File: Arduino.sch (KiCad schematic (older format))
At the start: 0 parts

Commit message: Hooked up top level schematic
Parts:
- added ARD?: ARDUINO_PINS, symbol ARDUINO_PINS
- added R? (x13): R, ~, symbol R
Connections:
- net MISO: now also R?.2
- net MOSI: now also R?.2
- net SCLK: now also R?.2
- net Tach_Meas: now also R?.1
- new net: ARD?.11 (DIGITAL_0_RX), R?.1
- new net: ARD?.12 (DIGITAL_1_TX), R?.1
- new net: ARD?.18 (DIGITAL_7), R?.1
- new net: ARD?.19 (DIGITAL_8), R?.1
- new net: ARD?.20 (DIGITAL_9_CS), R?.1
- new net: ARD?.21 (DIGITAL_10_MOSI), R?.1
- new net: ARD?.22 (DIGITAL_11_MISO), R?.1
- new net: ARD?.23 (DIGITAL_12_SCK), R?.1
- new net: ARD?.5 (ANALOG_0), R?.2
- new net: ARD?.6 (ANALOG_1), R?.2
- new net: ARD?.7 (ANALOG_2), R?.2
- new net: ARD?.8 (ANALOG_3), R?.2
- new net ADC_CS_N: R?.2
- new net CURR_MEAS: R?.1
- new net DAC_CS_N: R?.2
- new net Fan_En_N: R?.2
- new net GND: R?.1
- new net LED_EN_PWM: R?.2
- new net RELAY+: R?.2
- new net RELAY-: R?.2
- new net V+_ADJ_MON: R?.1
- new net V-_ADJ_MON: R?.1

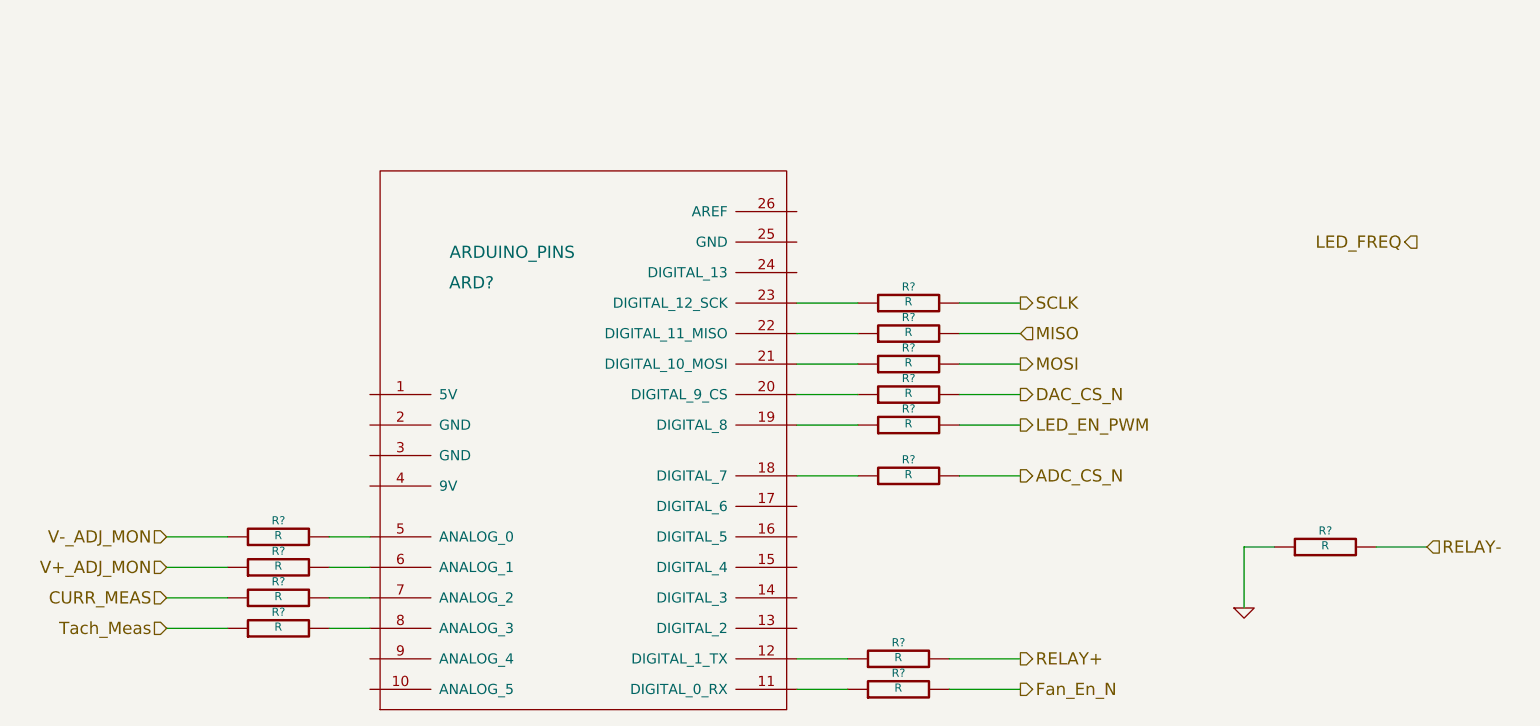
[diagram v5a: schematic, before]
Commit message: Fan Current module refactoring
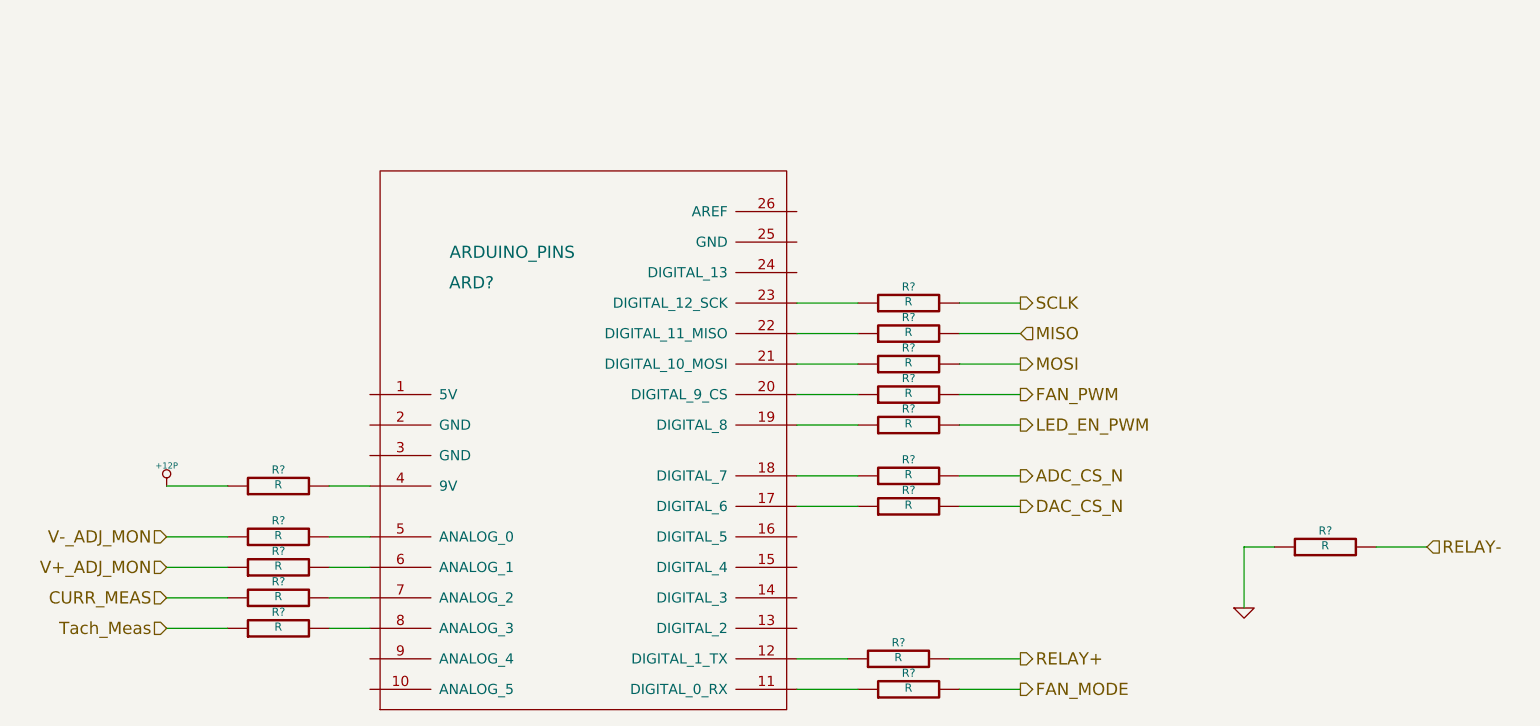
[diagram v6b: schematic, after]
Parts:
- removed R?: R, ~, symbol R
- added R? (x3): R, ~, symbol R
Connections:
- net at ARD?.11 (DIGITAL_0_RX): now also R?.1
- net at ARD?.17 (DIGITAL_6): now also R?.1
- net at ARD?.20 (DIGITAL_9_CS): now also R?.1; no longer R?.1
- net at ARD?.4 (9V): now also R?.2
- new net +12P: R?.1
- new net FAN_MODE: R?.2
- new net FAN_PWM: R?.2
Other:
- moved on the sheet: R?
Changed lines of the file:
@@
 Text HLabel 5900 3550 2    60   Output ~ 0
 SCLK
-Text HLabel 5900 4000 2    60   Output ~ 0
+Text HLabel 5900 4550 2    60   Output ~ 0
 DAC_CS_N
 Text HLabel 5900 4150 2    60   Output ~ 0
 LED_EN_PWM
-Text HLabel 7850 3250 0    60   Output ~ 0
-LED_FREQ
-Text HLabel 5900 5450 2    60   Output ~ 0
-Fan_En_N
 Text HLabel 1700 5150 0    60   Input ~ 0
 Tach_Meas
@@
 $Comp
 L R R?
-U 1 1 52F1858D
-P 5300 5450
-F 0 "R?" V 5380 5450 40  0000 C CNN
-F 1 "R" V 5307 5451 40  0000 C CNN
-F 2 "~" V 5230 5450 30  0000 C CNN
-F 3 "~" H 5300 5450 30  0000 C CNN
-	1    5300 5450
-	0    -1   -1   0
-$EndComp
-Wire Wire Line
-	4800 5450 5050 5450
-Wire Wire Line
-	5550 5450 5900 5450
-$Comp
-L R R?
 U 1 1 52F1A3E5
 P 5300 5300
@@
 L R R?
 U 1 1 52F1B48C
-P 5350 4000
-F 0 "R?" V 5430 4000 40  0000 C CNN
-F 1 "R" V 5357 4001 40  0000 C CNN
-F 2 "~" V 5280 4000 30  0000 C CNN
-F 3 "~" H 5350 4000 30  0000 C CNN
-	1    5350 4000
+P 5350 4550
+F 0 "R?" V 5430 4550 40  0000 C CNN
+F 1 "R" V 5357 4551 40  0000 C CNN
+F 2 "~" V 5280 4550 30  0000 C CNN
+F 3 "~" H 5350 4550 30  0000 C CNN
+	1    5350 4550
 	0    -1   -1   0
 $EndComp
@@
 	4800 3850 5100 3850
 Wire Wire Line
-	4800 4000 5100 4000
+	4800 4550 5100 4550
 Wire Wire Line
 	5600 3550 5900 3550
@@
 	5600 3850 5900 3850
 Wire Wire Line
-	5600 4000 5900 4000
+	5600 4550 5900 4550
 $Comp
 L R R?
@@
 Wire Wire Line
 	5600 4400 5900 4400
+$Comp
+L R R?
+U 1 1 52F170F5
+P 5350 4000
+F 0 "R?" V 5430 4000 40  0000 C CNN
+F 1 "R" V 5357 4001 40  0000 C CNN
+F 2 "~" V 5280 4000 30  0000 C CNN
+F 3 "~" H 5350 4000 30  0000 C CNN
+	1    5350 4000
+	0    -1   -1   0
+$EndComp
+Wire Wire Line
+	4800 4000 5100 4000
+Wire Wire Line
+	5600 4000 5900 4000
+Text HLabel 5900 4000 2    60   Output ~ 0
+FAN_PWM
+Text HLabel 5900 5450 2    60   Output ~ 0
+FAN_MODE
+$Comp
+L R R?
+U 1 1 52F19429
+P 5350 5450
+F 0 "R?" V 5430 5450 40  0000 C CNN
+F 1 "R" V 5357 5451 40  0000 C CNN
+F 2 "~" V 5280 5450 30  0000 C CNN
+F 3 "~" H 5350 5450 30  0000 C CNN
+	1    5350 5450
+	0    -1   -1   0
+$EndComp
+Wire Wire Line
+	4800 5450 5100 5450
+Wire Wire Line
+	5600 5450 5900 5450
+$Comp
+L R R?
+U 1 1 52F19431
+P 2250 4450
+F 0 "R?" V 2330 4450 40  0000 C CNN
+F 1 "R" V 2257 4451 40  0000 C CNN
+F 2 "~" V 2180 4450 30  0000 C CNN
+F 3 "~" H 2250 4450 30  0000 C CNN
+	1    2250 4450
+	0    -1   -1   0
+$EndComp
+Wire Wire Line
+	1700 4450 2000 4450
+Wire Wire Line
+	2500 4450 2700 4450
+$Comp
+L +12P #PWR?
+U 1 1 52F1943B
+P 1700 4450
+F 0 "#PWR?" H 1700 4420 30  0001 C CNN
+F 1 "+12P" H 1700 4550 30  0000 C CNN
+F 2 "" H 1700 4450 60  0000 C CNN
+F 3 "" H 1700 4450 60  0000 C CNN
+	1    1700 4450
+	1    0    0    -1
+$EndComp
 $EndSCHEMATC

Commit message: Begin Associating relay Module
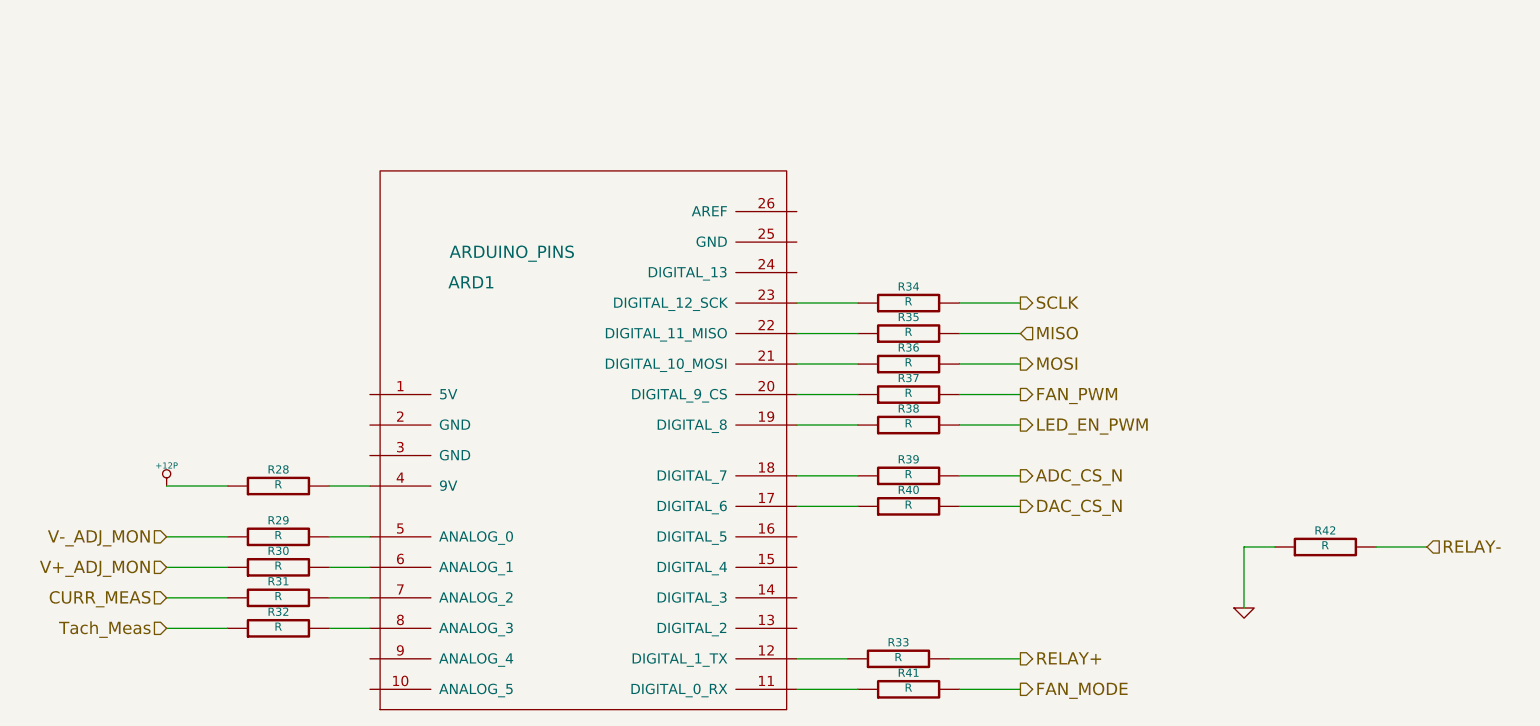
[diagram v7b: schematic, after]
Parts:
- gave numbers to parts that had none: 16
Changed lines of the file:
@@
 LIBS:BenchBudEE
 LIBS:BenchBudEE-cache
-EELAYER 27 0
+EELAYER 24 0
 EELAYER END
 $Descr A4 11693 8268
@@
 Tach_Meas
 $Comp
-L ARDUINO_PINS ARD?
+L ARDUINO_PINS ARD1
 U 1 1 52F1855D
 P 3650 5650
-F 0 "ARD?" H 3200 7850 60  0000 C CNN
+F 0 "ARD1" H 3200 7850 60  0000 C CNN
 F 1 "ARDUINO_PINS" H 3400 8000 60  0000 C CNN
 F 2 "" H 3650 5650 60  0000 C CNN
@@
 CURR_MEAS
 $Comp
-L R R?
+L R R33
 U 1 1 52F1A3E5
 P 5300 5300
-F 0 "R?" V 5380 5300 40  0000 C CNN
+F 0 "R33" V 5380 5300 40  0000 C CNN
 F 1 "R" V 5307 5301 40  0000 C CNN
 F 2 "~" V 5230 5300 30  0000 C CNN
@@
 	5550 5300 5900 5300
 $Comp
-L R R?
+L R R32
 U 1 1 52F1A3FE
 P 2250 5150
-F 0 "R?" V 2330 5150 40  0000 C CNN
+F 0 "R32" V 2330 5150 40  0000 C CNN
 F 1 "R" V 2257 5151 40  0000 C CNN
 F 2 "~" V 2180 5150 30  0000 C CNN
@@
 $EndComp
 $Comp
-L R R?
+L R R31
 U 1 1 52F1A404
 P 2250 5000
-F 0 "R?" V 2330 5000 40  0000 C CNN
+F 0 "R31" V 2330 5000 40  0000 C CNN
 F 1 "R" V 2257 5001 40  0000 C CNN
 F 2 "~" V 2180 5000 30  0000 C CNN
@@
 V-_ADJ_MON
 $Comp
-L R R?
+L R R30
 U 1 1 52F1B42B
 P 2250 4850
-F 0 "R?" V 2330 4850 40  0000 C CNN
+F 0 "R30" V 2330 4850 40  0000 C CNN
 F 1 "R" V 2257 4851 40  0000 C CNN
 F 2 "~" V 2180 4850 30  0000 C CNN
@@
 $EndComp
 $Comp
-L R R?
+L R R29
 U 1 1 52F1B431
 P 2250 4700
-F 0 "R?" V 2330 4700 40  0000 C CNN
+F 0 "R29" V 2330 4700 40  0000 C CNN
 F 1 "R" V 2257 4701 40  0000 C CNN
 F 2 "~" V 2180 4700 30  0000 C CNN
@@
 	2500 4850 2700 4850
 $Comp
-L R R?
+L R R34
 U 1 1 52F1B473
 P 5350 3550
-F 0 "R?" V 5430 3550 40  0000 C CNN
+F 0 "R34" V 5430 3550 40  0000 C CNN
 F 1 "R" V 5357 3551 40  0000 C CNN
 F 2 "~" V 5280 3550 30  0000 C CNN
@@
 $EndComp
 $Comp
-L R R?
+L R R35
 U 1 1 52F1B480
 P 5350 3700
-F 0 "R?" V 5430 3700 40  0000 C CNN
+F 0 "R35" V 5430 3700 40  0000 C CNN
 F 1 "R" V 5357 3701 40  0000 C CNN
 F 2 "~" V 5280 3700 30  0000 C CNN
@@
 $EndComp
 $Comp
-L R R?
+L R R36
 U 1 1 52F1B486
 P 5350 3850
-F 0 "R?" V 5430 3850 40  0000 C CNN
+F 0 "R36" V 5430 3850 40  0000 C CNN
 F 1 "R" V 5357 3851 40  0000 C CNN
 F 2 "~" V 5280 3850 30  0000 C CNN
@@
 $EndComp
 $Comp
-L R R?
+L R R40
 U 1 1 52F1B48C
 P 5350 4550
-F 0 "R?" V 5430 4550 40  0000 C CNN
+F 0 "R40" V 5430 4550 40  0000 C CNN
 F 1 "R" V 5357 4551 40  0000 C CNN
 F 2 "~" V 5280 4550 30  0000 C CNN
@@
 	5600 4550 5900 4550
 $Comp
-L R R?
+L R R42
 U 1 1 52F1B51A
 P 7400 4750
-F 0 "R?" V 7480 4750 40  0000 C CNN
+F 0 "R42" V 7480 4750 40  0000 C CNN
 F 1 "R" V 7407 4751 40  0000 C CNN
 F 2 "~" V 7330 4750 30  0000 C CNN
@@
 $EndComp
 $Comp
-L GND #PWR?
+L GND #PWR55
 U 1 1 52F1B529
 P 7000 5050
-F 0 "#PWR?" H 7000 5050 30  0001 C CNN
+F 0 "#PWR55" H 7000 5050 30  0001 C CNN
 F 1 "GND" H 7000 4980 30  0001 C CNN
 F 2 "" H 7000 5050 60  0000 C CNN
@@
 	7650 4750 7900 4750
 $Comp
-L R R?
+L R R38
 U 1 1 52F1B568
 P 5350 4150
-F 0 "R?" V 5430 4150 40  0000 C CNN
+F 0 "R38" V 5430 4150 40  0000 C CNN
 F 1 "R" V 5357 4151 40  0000 C CNN
 F 2 "~" V 5280 4150 30  0000 C CNN
@@
 	5600 4150 5900 4150
 $Comp
-L R R?
+L R R39
 U 1 1 52F27389
 P 5350 4400
-F 0 "R?" V 5430 4400 40  0000 C CNN
+F 0 "R39" V 5430 4400 40  0000 C CNN
 F 1 "R" V 5357 4401 40  0000 C CNN
 F 2 "~" V 5280 4400 30  0000 C CNN
@@
 	5600 4400 5900 4400
 $Comp
-L R R?
+L R R37
 U 1 1 52F170F5
 P 5350 4000
-F 0 "R?" V 5430 4000 40  0000 C CNN
+F 0 "R37" V 5430 4000 40  0000 C CNN
 F 1 "R" V 5357 4001 40  0000 C CNN
 F 2 "~" V 5280 4000 30  0000 C CNN
@@
 FAN_MODE
 $Comp
-L R R?
+L R R41
 U 1 1 52F19429
 P 5350 5450
-F 0 "R?" V 5430 5450 40  0000 C CNN
+F 0 "R41" V 5430 5450 40  0000 C CNN
 F 1 "R" V 5357 5451 40  0000 C CNN
 F 2 "~" V 5280 5450 30  0000 C CNN
@@
 	5600 5450 5900 5450
 $Comp
-L R R?
+L R R28
 U 1 1 52F19431
 P 2250 4450
-F 0 "R?" V 2330 4450 40  0000 C CNN
+F 0 "R28" V 2330 4450 40  0000 C CNN
 F 1 "R" V 2257 4451 40  0000 C CNN
 F 2 "~" V 2180 4450 30  0000 C CNN
@@
 	2500 4450 2700 4450
 $Comp
-L +12P #PWR?
+L +12P #PWR54
 U 1 1 52F1943B
 P 1700 4450
-F 0 "#PWR?" H 1700 4420 30  0001 C CNN
+F 0 "#PWR54" H 1700 4420 30  0001 C CNN
 F 1 "+12P" H 1700 4550 30  0000 C CNN
 F 2 "" H 1700 4450 60  0000 C CNN

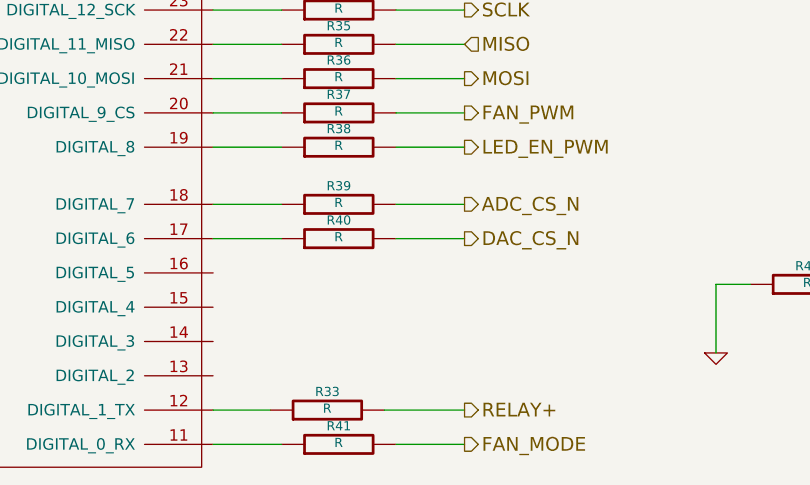
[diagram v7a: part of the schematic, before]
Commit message: Associated Thermocouple module
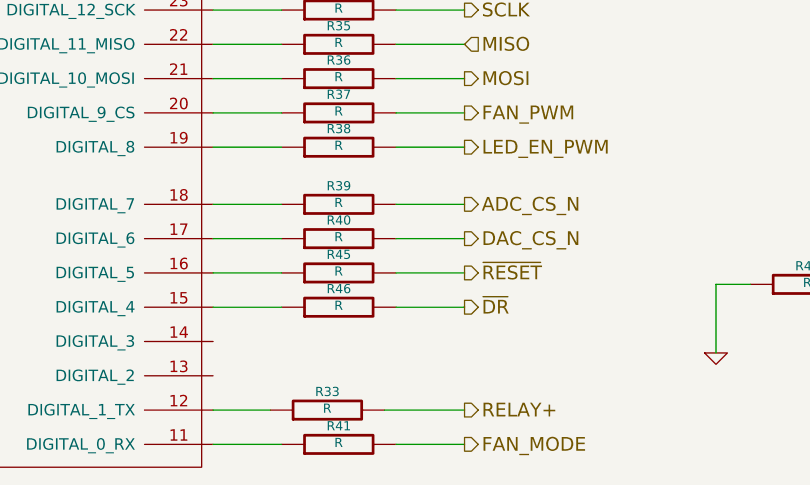
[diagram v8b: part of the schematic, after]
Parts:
- added R45, R46: R, ~, symbol R
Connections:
- net at ARD1.15 (DIGITAL_4): now also R46.1
- net at ARD1.16 (DIGITAL_5): now also R45.1
- new net ~DR: R46.2
- new net ~RESET: R45.2
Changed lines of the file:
@@
 $EndComp
 $Comp
-L GND #PWR55
+L GND #PWR059
 U 1 1 52F1B529
 P 7000 5050
-F 0 "#PWR55" H 7000 5050 30  0001 C CNN
+F 0 "#PWR059" H 7000 5050 30  0001 C CNN
 F 1 "GND" H 7000 4980 30  0001 C CNN
 F 2 "" H 7000 5050 60  0000 C CNN
@@
 	2500 4450 2700 4450
 $Comp
-L +12P #PWR54
+L +12P #PWR060
 U 1 1 52F1943B
 P 1700 4450
-F 0 "#PWR54" H 1700 4420 30  0001 C CNN
+F 0 "#PWR060" H 1700 4420 30  0001 C CNN
 F 1 "+12P" H 1700 4550 30  0000 C CNN
 F 2 "" H 1700 4450 60  0000 C CNN
@@
 	1    0    0    -1
 $EndComp
+Text HLabel 5900 4850 2    60   Output ~ 0
+~DR
+$Comp
+L R R46
+U 1 1 53038239
+P 5350 4850
+F 0 "R46" V 5430 4850 40  0000 C CNN
+F 1 "R" V 5357 4851 40  0000 C CNN
+F 2 "~" V 5280 4850 30  0000 C CNN
+F 3 "~" H 5350 4850 30  0000 C CNN
+	1    5350 4850
+	0    -1   -1   0
+$EndComp
+Wire Wire Line
+	4800 4850 5100 4850
+Wire Wire Line
+	5600 4850 5900 4850
+Text HLabel 5900 4700 2    60   Output ~ 0
+~RESET
+$Comp
+L R R45
+U 1 1 53038242
+P 5350 4700
+F 0 "R45" V 5430 4700 40  0000 C CNN
+F 1 "R" V 5357 4701 40  0000 C CNN
+F 2 "~" V 5280 4700 30  0000 C CNN
+F 3 "~" H 5350 4700 30  0000 C CNN
+	1    5350 4700
+	0    -1   -1   0
+$EndComp
+Wire Wire Line
+	4800 4700 5100 4700
+Wire Wire Line
+	5600 4700 5900 4700
 $EndSCHEMATC
